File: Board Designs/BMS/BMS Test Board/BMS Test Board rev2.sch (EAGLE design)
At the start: 35 parts, among them IC1 OKI-78SR-5, IC2 NE5532SOIC

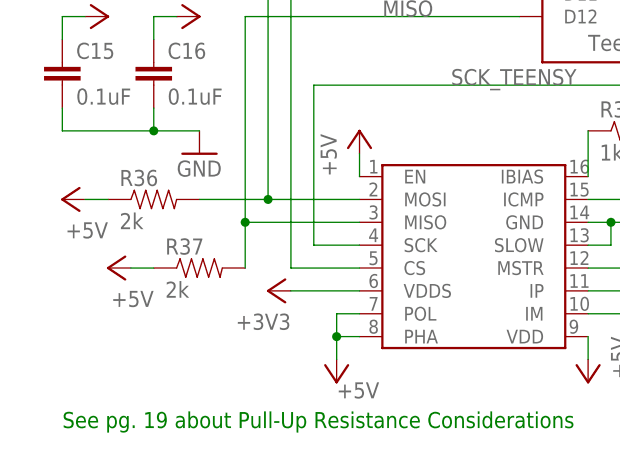
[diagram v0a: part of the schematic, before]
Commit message: Tweaked BMS test board, added rev2 with swapped SPI mode resistors
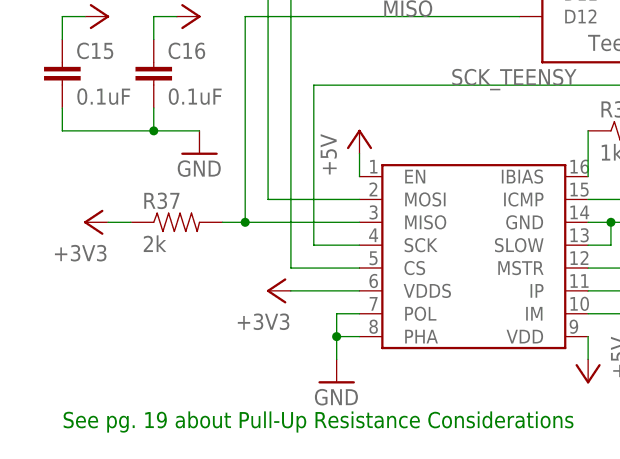
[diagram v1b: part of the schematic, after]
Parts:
- removed R36: 2k, HyTechDevices:RESISTOR0805-RES
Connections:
- net +3V3: now also R37.1
- net +5V: no longer R36.1, R37.1, U$8.PHA, U$8.POL
- net GND: now also U$8.PHA, U$8.POL
- net MOSI_TEENSY: no longer R36.2
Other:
- moved on the sheet: R37
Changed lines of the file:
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@@
 <part name="GND15" library="supply1" deviceset="GND" device=""/>
 <part name="U$8" library="HyTechDevices" deviceset="LTC6820" device=""/>
-<part name="P+13" library="supply1" deviceset="+5V" device=""/>
 <part name="P+17" library="supply1" deviceset="+5V" device=""/>
 <part name="R33" library="HyTechDevices" deviceset="RESISTOR" device="0805-RES" value="1k"/>
@@
 <part name="C4" library="HyTechDevices" deviceset="CAP" device="0805" value="27pF"/>
 <part name="GND22" library="HyTechSymbols" deviceset="GND" device=""/>
-<part name="R36" library="HyTechDevices" deviceset="RESISTOR" device="0805-RES" value="2k"/>
 <part name="R37" library="HyTechDevices" deviceset="RESISTOR" device="0805-RES" value="2k"/>
-<part name="P+19" library="supply1" deviceset="+5V" device=""/>
-<part name="P+20" library="supply1" deviceset="+5V" device=""/>
 <part name="U$9" library="HyTechDevices" deviceset="TEENSY_3.2_SIMPLE" device=""/>
 <part name="GND24" library="supply1" library_urn="urn:adsk.eagle:library:371" deviceset="GND" device=""/>
@@
 <part name="P+9" library="supply1" deviceset="+5V" device=""/>
 <part name="+3V6" library="supply1" library_urn="urn:adsk.eagle:library:371" deviceset="+3V3" device=""/>
+<part name="+3V4" library="supply1" library_urn="urn:adsk.eagle:library:371" deviceset="+3V3" device=""/>
+<part name="GND2" library="HyTechSymbols" deviceset="GND" device=""/>
 </parts>
 <sheets>
@@
 </instance>
 <instance part="U$8" gate="G$1" x="60.96" y="-137.16" smashed="yes"/>
-<instance part="P+13" gate="1" x="45.72" y="-152.4" smashed="yes" rot="MR180">
-<attribute name="VALUE" x="45.72" y="-152.4" size="1.778" layer="96" rot="MR180"/>
-</instance>
 <instance part="P+17" gate="1" x="73.66" y="-152.4" smashed="yes" rot="R180">
 <attribute name="VALUE" x="76.2" y="-147.32" size="1.778" layer="96" rot="R270"/>
@@
 <attribute name="VALUE" x="93.98" y="-129.54" size="1.778" layer="96" rot="R180"/>
 </instance>
-<instance part="R36" gate="G$1" x="25.4" y="-132.08" smashed="yes">
-<attribute name="NAME" x="21.59" y="-130.5814" size="1.778" layer="95"/>
-<attribute name="VALUE" x="21.59" y="-135.382" size="1.778" layer="96"/>
-</instance>
-<instance part="R37" gate="G$1" x="30.48" y="-139.7" smashed="yes">
-<attribute name="NAME" x="26.67" y="-138.2014" size="1.778" layer="95"/>
-<attribute name="VALUE" x="26.67" y="-143.002" size="1.778" layer="96"/>
-</instance>
-<instance part="P+19" gate="1" x="15.24" y="-132.08" smashed="yes" rot="R90">
-<attribute name="VALUE" x="20.32" y="-134.62" size="1.778" layer="96" rot="R180"/>
-</instance>
-<instance part="P+20" gate="1" x="20.32" y="-139.7" smashed="yes" rot="R90">
-<attribute name="VALUE" x="25.4" y="-142.24" size="1.778" layer="96" rot="R180"/>
+<instance part="R37" gate="G$1" x="27.94" y="-134.62" smashed="yes">
+<attribute name="NAME" x="24.13" y="-133.1214" size="1.778" layer="95"/>
+<attribute name="VALUE" x="24.13" y="-137.922" size="1.778" layer="96"/>
 </instance>
 <instance part="U$9" gate="G$1" x="68.58" y="-116.84" smashed="yes"/>
@@
 <instance part="+3V6" gate="G$1" x="20.32" y="-111.76" smashed="yes" rot="R270">
 <attribute name="VALUE" x="17.78" y="-109.22" size="1.778" layer="96"/>
+</instance>
+<instance part="+3V4" gate="G$1" x="17.78" y="-134.62" smashed="yes" rot="R90">
+<attribute name="VALUE" x="20.32" y="-137.16" size="1.778" layer="96" rot="R180"/>
+</instance>
+<instance part="GND2" gate="1" x="45.72" y="-152.4" smashed="yes">
+<attribute name="VALUE" x="43.18" y="-154.94" size="1.778" layer="96"/>
 </instance>
 </instances>
@@
 <wire x1="30.48" y1="-124.46" x2="25.4" y2="-124.46" width="0.1524" layer="91"/>
 </segment>
+<segment>
+<pinref part="U$8" gate="G$1" pin="POL"/>
+<pinref part="U$8" gate="G$1" pin="PHA"/>
+<wire x1="48.26" y1="-144.78" x2="45.72" y2="-144.78" width="0.1524" layer="91"/>
+<wire x1="45.72" y1="-144.78" x2="45.72" y2="-147.32" width="0.1524" layer="91"/>
+<wire x1="45.72" y1="-147.32" x2="48.26" y2="-147.32" width="0.1524" layer="91"/>
+<wire x1="45.72" y1="-147.32" x2="45.72" y2="-149.86" width="0.1524" layer="91"/>
+<junction x="45.72" y="-147.32"/>
+<pinref part="GND2" gate="1" pin="GND"/>
+</segment>
 </net>
 <net name="+12V" class="0">
@@
 <pinref part="P+17" gate="1" pin="+5V"/>
 <wire x1="73.66" y1="-147.32" x2="73.66" y2="-149.86" width="0.1524" layer="91"/>
-</segment>
-<segment>
-<pinref part="R36" gate="G$1" pin="1"/>
-<pinref part="P+19" gate="1" pin="+5V"/>
-<wire x1="17.78" y1="-132.08" x2="20.32" y2="-132.08" width="0.1524" layer="91"/>
-</segment>
-<segment>
-<pinref part="R37" gate="G$1" pin="1"/>
-<pinref part="P+20" gate="1" pin="+5V"/>
-<wire x1="22.86" y1="-139.7" x2="25.4" y2="-139.7" width="0.1524" layer="91"/>
 </segment>
 <segment>
@@
 <pinref part="P+25" gate="1" pin="+5V"/>
 <wire x1="48.26" y1="-129.54" x2="48.26" y2="-127" width="0.1524" layer="91"/>
-</segment>
-<segment>
-<pinref part="U$8" gate="G$1" pin="POL"/>
-<pinref part="U$8" gate="G$1" pin="PHA"/>
-<pinref part="P+13" gate="1" pin="+5V"/>
-<wire x1="48.26" y1="-144.78" x2="45.72" y2="-144.78" width="0.1524" layer="91"/>
-<wire x1="45.72" y1="-144.78" x2="45.72" y2="-147.32" width="0.1524" layer="91"/>
-<wire x1="45.72" y1="-147.32" x2="48.26" y2="-147.32" width="0.1524" layer="91"/>
-<wire x1="45.72" y1="-147.32" x2="45.72" y2="-149.86" width="0.1524" layer="91"/>
-<junction x="45.72" y="-147.32"/>
 </segment>
 <segment>
@@
 <wire x1="48.26" y1="-134.62" x2="35.56" y2="-134.62" width="0.1524" layer="91"/>
 <wire x1="35.56" y1="-134.62" x2="35.56" y2="-111.76" width="0.1524" layer="91"/>
-<wire x1="35.56" y1="-134.62" x2="35.56" y2="-139.7" width="0.1524" layer="91"/>
+<wire x1="35.56" y1="-134.62" x2="33.02" y2="-134.62" width="0.1524" layer="91"/>
 <junction x="35.56" y="-134.62"/>
 <pinref part="R37" gate="G$1" pin="2"/>
@@
 <wire x1="15.24" y1="-111.76" x2="15.24" y2="-114.3" width="0.1524" layer="91"/>
 </segment>
+<segment>
+<pinref part="R37" gate="G$1" pin="1"/>
+<wire x1="20.32" y1="-134.62" x2="22.86" y2="-134.62" width="0.1524" layer="91"/>
+<pinref part="+3V4" gate="G$1" pin="+3V3"/>
+</segment>
 </net>
 <net name="CS_MCP3208_3.3V" class="0">
@@
 <wire x1="48.26" y1="-132.08" x2="38.1" y2="-132.08" width="0.1524" layer="91"/>
 <wire x1="38.1" y1="-132.08" x2="38.1" y2="-109.22" width="0.1524" layer="91"/>
-<pinref part="R36" gate="G$1" pin="2"/>
-<wire x1="38.1" y1="-132.08" x2="30.48" y2="-132.08" width="0.1524" layer="91"/>
-<junction x="38.1" y="-132.08"/>
 <pinref part="U$9" gate="G$1" pin="D11"/>
 <wire x1="38.1" y1="-109.22" x2="66.04" y2="-109.22" width="0.1524" layer="91"/>
